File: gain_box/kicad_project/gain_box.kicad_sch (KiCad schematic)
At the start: 98 parts, among them J1 Conn_01x02, J10 AVR-UPDI-6, J11 Conn_01x02, J2 Conn_01x02, J3 Conn_01x02, J4 Conn_01x02, J5 Conn_01x02, J6 Conn_01x02, J7 Conn_01x02, J8 Conn_01x02, J9 Conn_01x02, K1 G5V-1, K2 G5V-1, K3 G5V-1, K4 J107F1CS2012VDC.80, K5 J107F1CS2012VDC.80, Q1 AO3400A, Q2 AO3400A, Q3 AO3400A, T1 70042K, U1 NE5532, U10 140817141310, U2 NE5532, U3 NE5532, U4 LM7809, U5 LM7909, U6 LM7805_TO220, U7 ATtiny412-SS, U9 140817141310

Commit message: gain_box: preliminary amp section layout
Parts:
- removed R1: 100, Resistor_THT:R_Axial_DIN0204_L3.6mm_D1.6mm_P7.62mm_Horizontal, symbol Device:R
- removed RN1: 4x10K, Resistor_SMD:R_Array_Convex_4x1206, symbol Device:R_Pack04
- added C26, C27: 10u, Capacitor_THT:CP_Radial_D5.0mm_P2.00mm, symbol Device:C_Polarized
- added R25, R26: 33k, Resistor_SMD:R_0805_2012Metric_Pad1.20x1.40mm_HandSolder, symbol Device:R
- added R27, R28, R29, R30: 10k, Resistor_SMD:R_0805_2012Metric_Pad1.20x1.40mm_HandSolder, symbol Device:R
- added RV4: 300VAC, Varistor:RV_Disc_D9mm_W4.5mm_P5mm, symbol Device:Varistor
- added TP1, TP10, TP11, TP12, TP13, TP14, TP2, TP3, TP4, TP5, TP6, TP7, TP8, TP9: TestPoint, TestPoint:TestPoint_Pad_D2.0mm, symbol Connector:TestPoint
- C1, C2, C3: footprint Capacitor_THT:C_Rect_L26.5mm_W10.5mm_P22.50mm_MKS4 -> Capacitor_THT:C_Rect_L7.2mm_W4.5mm_P5.00mm_FKS2_FKP2_MKS2_MKP2
- C10, C11, C12, C13, C14, C15, C16, C17, C18: footprint (none) -> Capacitor_THT:C_Disc_D3.8mm_W2.6mm_P2.50mm
- C19: value 0.33u -> 330n; footprint (none) -> Capacitor_THT:C_Disc_D7.5mm_W4.4mm_P5.00mm; symbol Device:C_Polarized -> Device:C
- C20, C21, C22, C23: footprint (none) -> Capacitor_THT:CP_Radial_D16.0mm_P7.50mm
- C24, C25: footprint (none) -> Capacitor_THT:CP_Radial_D5.0mm_P2.00mm
- C4, C5, C6: footprint (none) -> Capacitor_THT:C_Rect_L7.2mm_W2.5mm_P5.00mm_FKS2_FKP2_MKS2_MKP2
- C7, C8, C9: footprint (none) -> Capacitor_THT:C_Rect_L13.0mm_W6.0mm_P10.00mm_FKS3_FKP3_MKS4
- J11: symbol Connector_Generic:Conn_01x03 -> Connector_Generic:Conn_01x02
- K1, K2: value G5V-1 -> J104D2C12VDC.36S
- K4: footprint gain_box:RELAY_SRD-05VDC-SL-C -> gain_box:RELAY_SRD-C
- K5: value J107F1CS2012VDC.80 -> J104D2C12VDC.36S
- R10, R11, R12, R13, R14, R15, R2, R22, R23, R24, R3, R4, R5, R6, R7, R8, R9: footprint Resistor_THT:R_Axial_DIN0204_L3.6mm_D1.6mm_P7.62mm_Horizontal -> Resistor_THT:R_Axial_DIN0207_L6.3mm_D2.5mm_P7.62mm_Horizontal
- R20, R21: value 2.2k -> 10k
- U6: value LM7805_TO220 -> 78L05; footprint Package_TO_SOT_THT:TO-220-3_Vertical -> Package_TO_SOT_SMD:SOT-89-3; symbol Regulator_Linear:LM7805_TO220 -> Regulator_Linear:L78L05_SOT89
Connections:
- net +12V: now also U6.3 (IN), C26.1, C27.1, TP4.1; no longer U6.1 (VI)
- net +5V: now also U6.1 (OUT), R27.1, TP5.1; no longer U6.3 (VO)
- net AC_EN: now also R28.1, TP9.1
- net AC_EN_G: now also TP12.1
- net AC_L: now also RV4.1
- net AC_N: now also RV4.2
- net AGND: now also TP2.1
- net AV+: now also TP1.1
- net AV-: now also TP3.1
- net EXTTRIG: now also TP7.1
- net GND: now also C26.2, C27.2, R25.1, R26.1, R28.2, R29.2, R30.2, TP6.1
- net TRIG: now also R30.1, TP11.1
- net TRIG_G: now also TP14.1
- net UNMUTE: now also R29.1, TP10.1
- net UNMUTE_G: now also TP13.1
- net UPDI: now also R27.2
- net TGO2: now reaches J9.2 (Pin_2), K5.14
- net TGO2: now also R26.2
- net TGO1: now reaches J8.2 (Pin_2), K5.24
- net TGO1: now also R25.2
- net at F1.1: now also J11.2 (Pin_2); no longer J11.3 (Pin_3)
- net AC_OK renamed AC_PULSE
- net AC_PULSE: now also TP8.1
- net AC_SENSE_1 renamed AC_SENSE
- no-connect marks 9 -> 8
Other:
- note added: "Trigger outputs"
- moved on the sheet: C13, C14, D5, D6, F1, K5, Q1, Q2, Q3, R18, R20, U6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

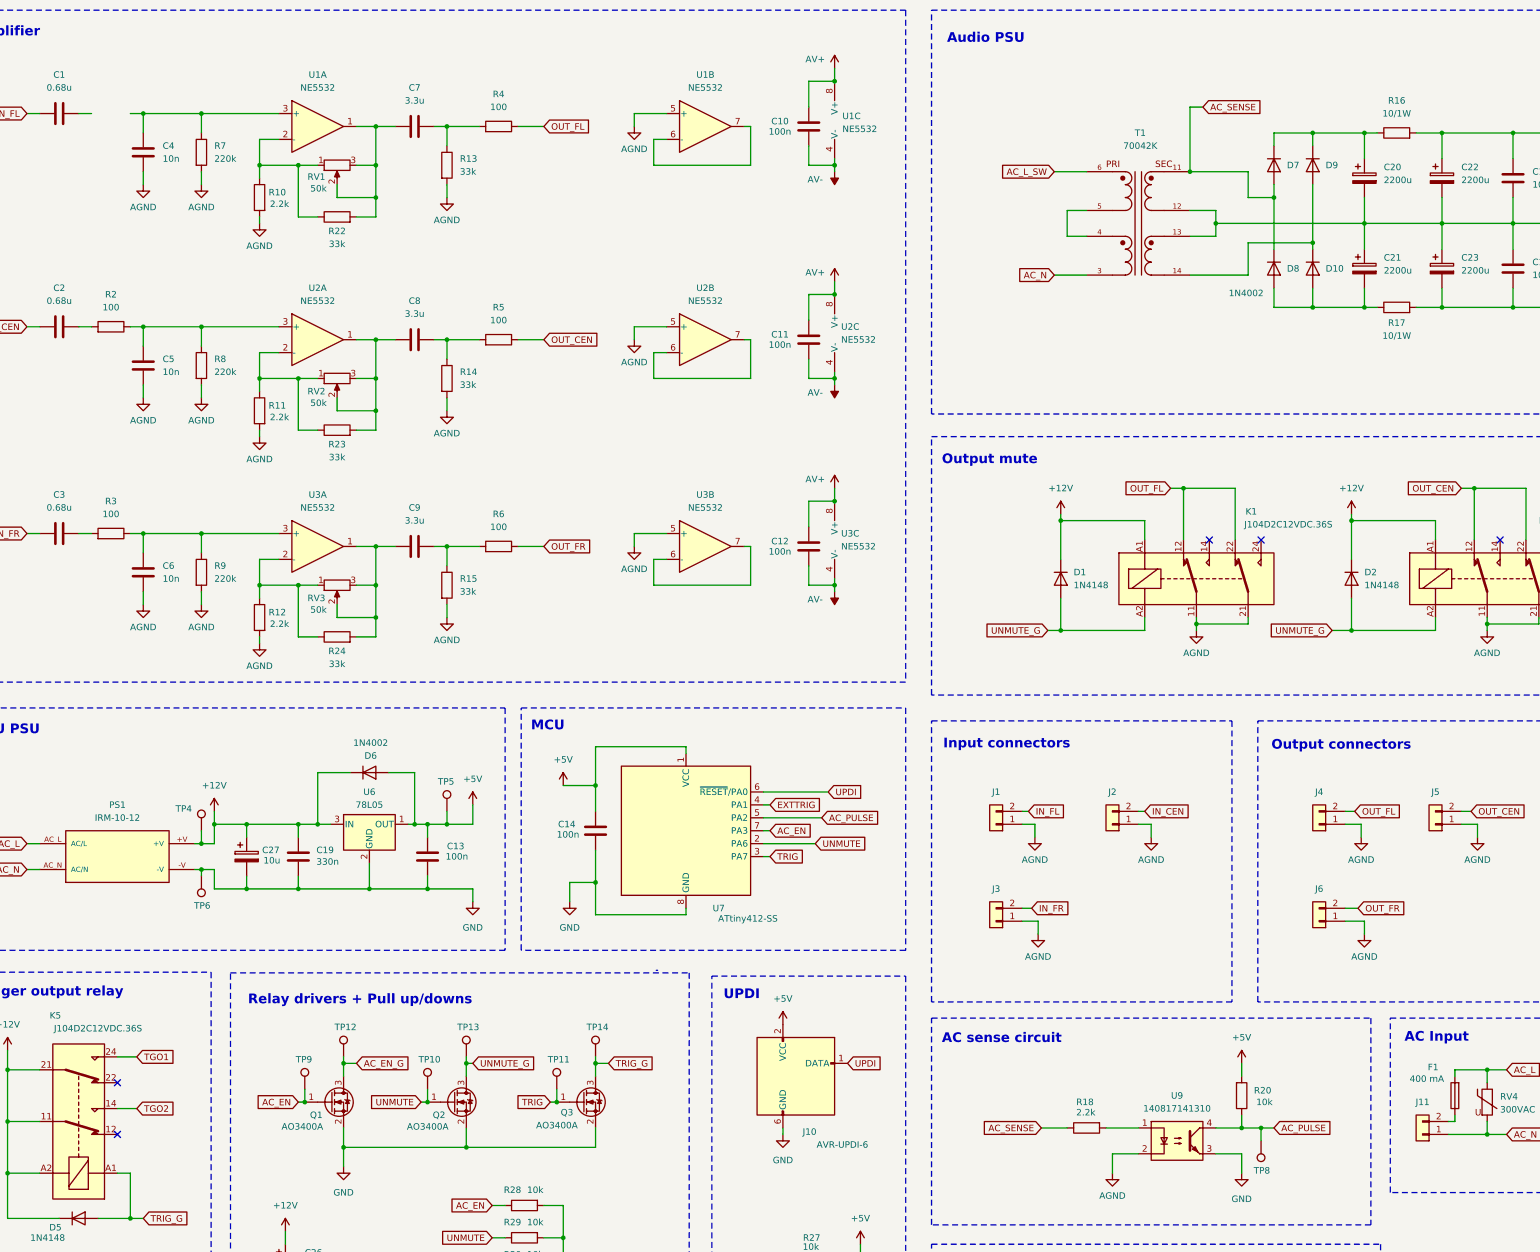
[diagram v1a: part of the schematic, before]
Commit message: gain_box: first audio PSU layout
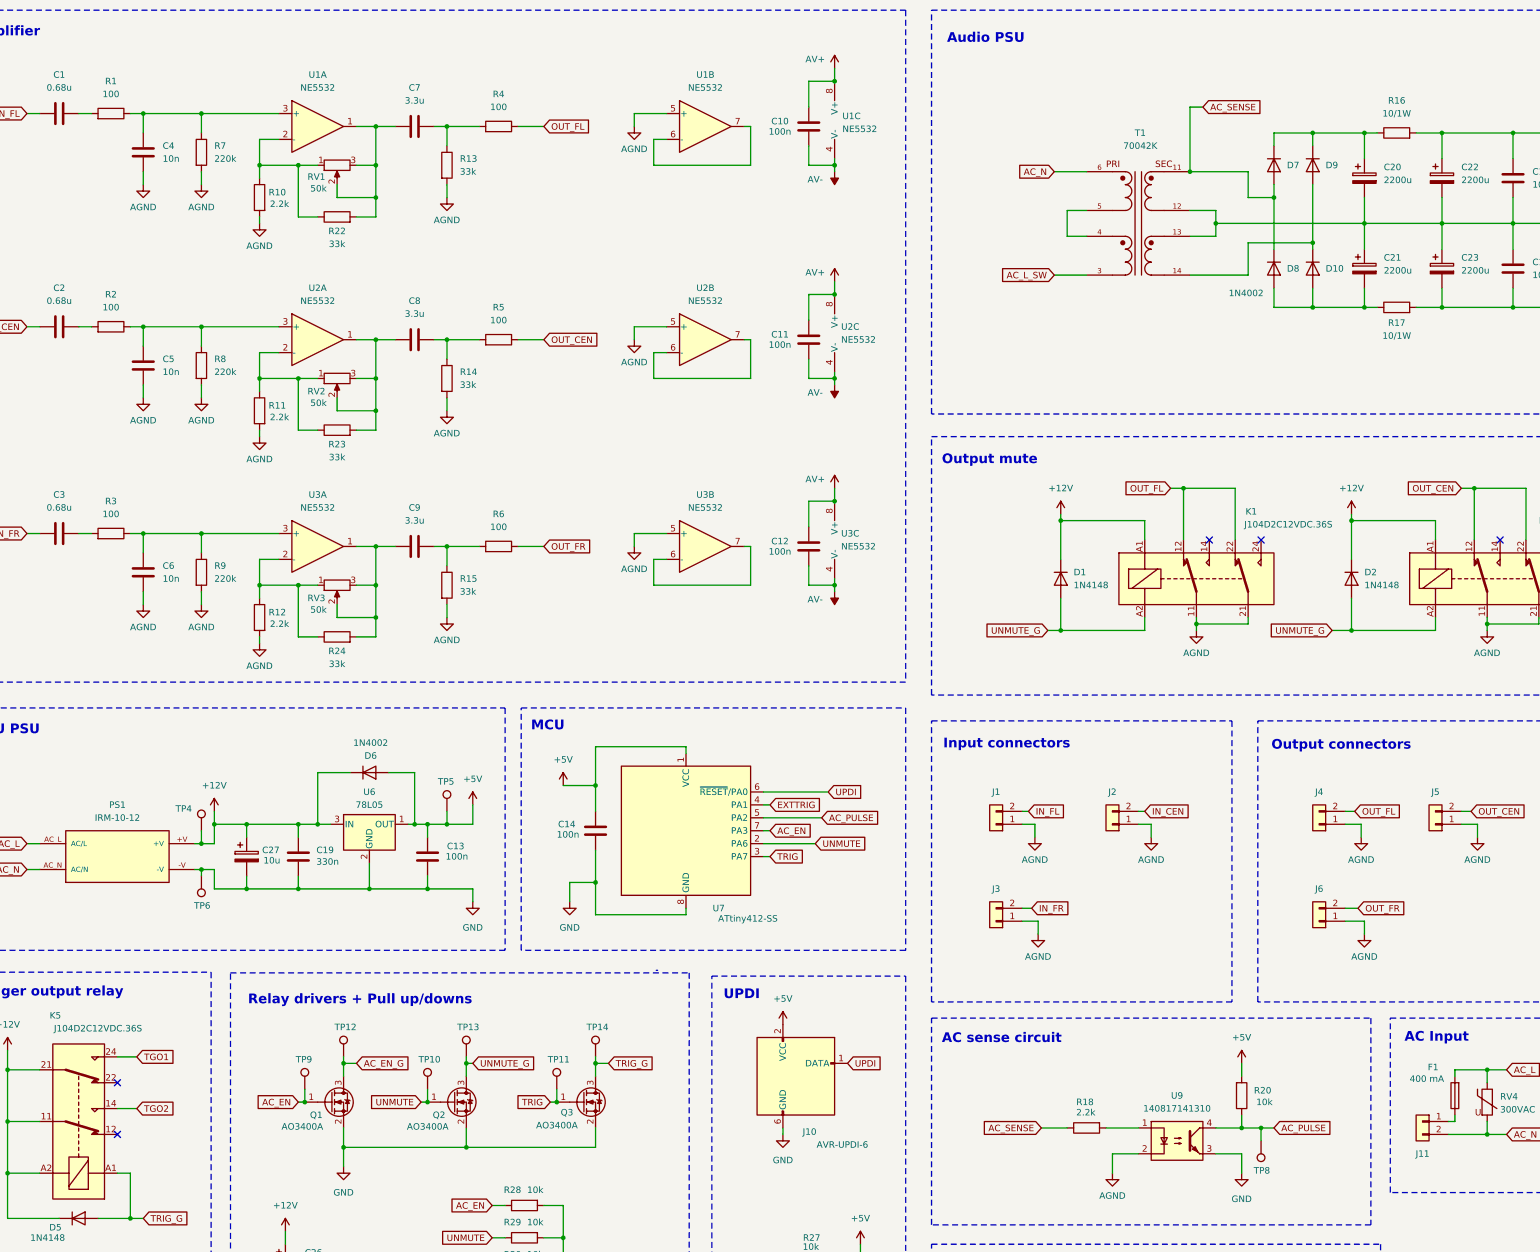
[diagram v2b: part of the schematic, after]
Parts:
- added R1: 100, Resistor_THT:R_Axial_DIN0207_L6.3mm_D2.5mm_P7.62mm_Horizontal, symbol Device:R
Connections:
- net AC_L_SW: now also T1.3; no longer T1.6
- net AC_N: now also J11.2 (Pin_2), T1.6; no longer J11.1 (Pin_1), T1.3
- net at C4.2, R7.1, U1.3 (+): now also R1.1
- net at F1.1: now also J11.1 (Pin_1); no longer J11.2 (Pin_2)
- net at C1.2: now also R1.2
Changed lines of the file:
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@@
 		)
 	)
+	(global_label "AC_L_SW"
+		(shape input)
+		(at 232.41 68.58 180)
+		(fields_autoplaced yes)
+		(effects
+			(font
+				(size 1.27 1.27)
+			)
+			(justify right)
+		)
+		(property "Intersheetrefs" "${INTERSHEET_REFS}"
+			(at 221.442 68.58 0)
+			(effects
+				(font
+					(size 1.27 1.27)
+				)
+				(justify right)
+				(hide yes)
+			)
+		)
+	)
 	(global_label "TGO1"
 		(shape input)
@@
 		)
 	)
-	(global_label "AC_L_SW"
-		(shape input)
-		(at 232.41 48.26 180)
-		(fields_autoplaced yes)
-		(effects
-			(font
-				(size 1.27 1.27)
-			)
-			(justify right)
-		)
-		(property "Intersheetrefs" "${INTERSHEET_REFS}"
-			(at 221.442 48.26 0)
-			(effects
-				(font
-					(size 1.27 1.27)
-				)
-				(justify right)
-				(hide yes)
-			)
-		)
-	)
 	(global_label "AC_L"
 		(shape input)
@@
 		)
 	)
-	(global_label "AC_N"
-		(shape input)
-		(at 232.41 68.58 180)
-		(fields_autoplaced yes)
-		(effects
-			(font
-				(size 1.27 1.27)
-			)
-			(justify right)
-		)
-		(property "Intersheetrefs" "${INTERSHEET_REFS}"
-			(at 224.7681 68.58 0)
-			(effects
-				(font
-					(size 1.27 1.27)
-				)
-				(justify right)
-				(hide yes)
-			)
-		)
-	)
 	(global_label "IN_CEN"
 		(shape input)
@@
 		)
 	)
+	(global_label "AC_N"
+		(shape input)
+		(at 232.41 48.26 180)
+		(fields_autoplaced yes)
+		(effects
+			(font
+				(size 1.27 1.27)
+			)
+			(justify right)
+		)
+		(property "Intersheetrefs" "${INTERSHEET_REFS}"
+			(at 224.7681 48.26 0)
+			(effects
+				(font
+					(size 1.27 1.27)
+				)
+				(justify right)
+				(hide yes)
+			)
+		)
+	)
 	(global_label "AC_PULSE"
 		(shape input)
@@
 	)
 	(symbol
+		(lib_id "Connector_Generic:Conn_01x02")
+		(at 304.8 234.95 0)
+		(mirror y)
+		(unit 1)
+		(exclude_from_sim no)
+		(in_bom yes)
+		(on_board yes)
+		(dnp no)
+		(property "Reference" "J11"
+			(at 304.8 241.3 0)
+			(effects
+				(font
+					(size 1.27 1.27)
+				)
+			)
+		)
+		(property "Value" "Conn_01x02"
+			(at 302.26 237.4899 0)
+			(effects
+				(font
+					(size 1.27 1.27)
+				)
+				(justify left)
+				(hide yes)
+			)
+		)
+		(property "Footprint" "Connector_JST:JST_VH_B2P3-VH_1x02_P7.92mm_Vertical"
+			(at 304.8 234.95 0)
+			(effects
+				(font
+					(size 1.27 1.27)
+				)
+				(hide yes)
+			)
+		)
+		(property "Datasheet" "~"
+			(at 304.8 234.95 0)
+			(effects
+				(font
+					(size 1.27 1.27)
+				)
+				(hide yes)
+			)
+		)
+		(property "Description" "Generic connector, single row, 01x02, script generated (kicad-library-utils/schlib/autogen/connector/)"
+			(at 304.8 234.95 0)
+			(effects
+				(font
+					(size 1.27 1.27)
+				)
+				(hide yes)
+			)
+		)
+		(pin "1"
+		)
+		(pin "2"
+		)
+		(instances
+			(project "gain_box"
+				(path "/9bac93c0-f586-4b1c-8172-4868afdb9131"
+					(reference "J11")
+					(unit 1)
+				)
+			)
+		)
+	)
+	(symbol
 		(lib_id "power:+12V")
 		(at 194.31 259.08 0)
@@
 	(symbol
 		(lib_id "Device:R")
+		(at 46.99 36.83 270)
+		(mirror x)
+		(unit 1)
+		(exclude_from_sim no)
+		(in_bom yes)
+		(on_board yes)
+		(dnp no)
+		(property "Reference" "R1"
+			(at 46.99 30.48 90)
+			(effects
+				(font
+					(size 1.27 1.27)
+				)
+			)
+		)
+		(property "Value" "100"
+			(at 46.99 33.02 90)
+			(effects
+				(font
+					(size 1.27 1.27)
+				)
+			)
+		)
+		(property "Footprint" "Resistor_THT:R_Axial_DIN0207_L6.3mm_D2.5mm_P7.62mm_Horizontal"
+			(at 46.99 38.608 90)
+			(effects
+				(font
+					(size 1.27 1.27)
+				)
+				(hide yes)
+			)
+		)
+		(property "Datasheet" "~"
+			(at 46.99 36.83 0)
+			(effects
+				(font
+					(size 1.27 1.27)
+				)
+				(hide yes)
+			)
+		)
+		(property "Description" "Resistor"
+			(at 46.99 36.83 0)
+			(effects
+				(font
+					(size 1.27 1.27)
+				)
+				(hide yes)
+			)
+		)
+		(pin "1"
+		)
+		(pin "2"
+		)
+		(instances
+			(project "gain_box"
+				(path "/9bac93c0-f586-4b1c-8172-4868afdb9131"
+					(reference "R1")
+					(unit 1)
+				)
+			)
+		)
+	)
+	(symbol
+		(lib_id "Device:R")
 		(at 185.42 262.89 270)
 		(mirror x)
@@
 					(unit 1)
 				)
-			)
-		)
-	)
-	(symbol
-		(lib_id "Connector_Generic:Conn_01x02")
-		(at 304.8 237.49 180)
-		(unit 1)
-		(exclude_from_sim no)
-		(in_bom yes)
-		(on_board yes)
-		(dnp no)
-		(fields_autoplaced yes)
-		(property "Reference" "J11"
-			(at 304.8 231.14 0)
-			(effects
-				(font
-					(size 1.27 1.27)
-				)
-			)
-		)
-		(property "Value" "Conn_01x02"
-			(at 302.26 234.9501 0)
-			(effects
-				(font
-					(size 1.27 1.27)
-				)
-				(justify left)
-				(hide yes)
-			)
-		)
-		(property "Footprint" "Connector_JST:JST_VH_B2P3-VH_1x02_P7.92mm_Vertical"
-			(at 304.8 237.49 0)
-			(effects
-				(font
-					(size 1.27 1.27)
-				)
-				(hide yes)
-			)
-		)
-		(property "Datasheet" "~"
-			(at 304.8 237.49 0)
-			(effects
-				(font
-					(size 1.27 1.27)
-				)
-				(hide yes)
-			)
-		)
-		(property "Description" "Generic connector, single row, 01x02, script generated (kicad-library-utils/schlib/autogen/connector/)"
-			(at 304.8 237.49 0)
-			(effects
-				(font
-					(size 1.27 1.27)
-				)
-				(hide yes)
-			)
-		)
-		(pin "1"
-		)
-		(pin "2"
-		)
-		(instances
-			(project "gain_box"
-				(path "/9bac93c0-f586-4b1c-8172-4868afdb9131"
-					(reference "J11")
-					(unit 1)
-				)
